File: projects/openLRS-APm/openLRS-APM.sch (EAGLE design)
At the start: 23 parts, among them IC2 RFM23BPSMD, J1 AVR_SPI_PRG_6PTH, U1 ATMEGA328P, Y1 16MHz

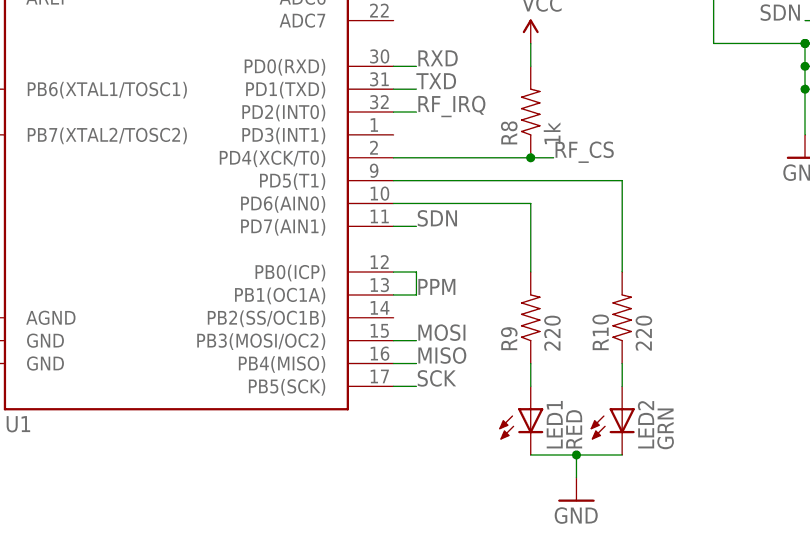
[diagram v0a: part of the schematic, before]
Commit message: Revert 0493923..5027763
This rolls back to commit 049392304cea7ab2cd1e886349edb191a1876f4a.
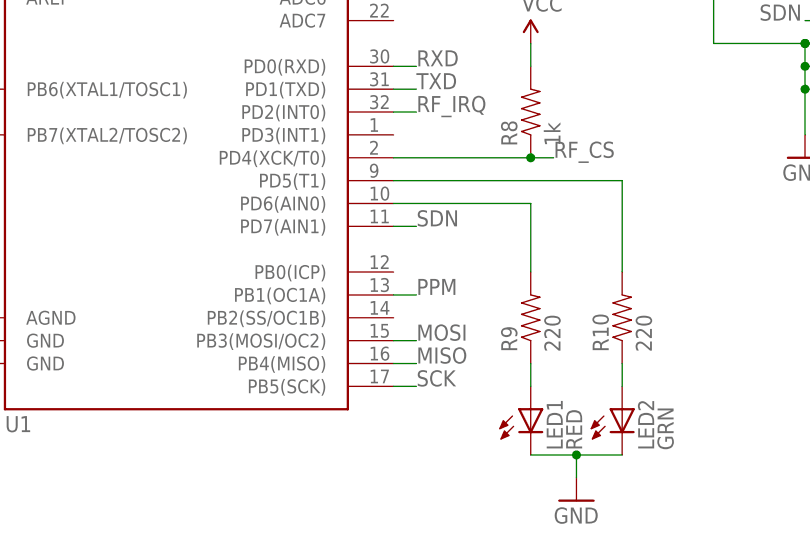
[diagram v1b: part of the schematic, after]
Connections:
- net PPM: no longer U1.PB0(ICP)
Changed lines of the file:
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@@
 <wire x1="91.44" y1="43.18" x2="93.98" y2="43.18" width="0.1524" layer="91"/>
 <label x="93.98" y="43.18" size="1.778" layer="95"/>
-<pinref part="U1" gate="G$1" pin="PB0(ICP)"/>
-<wire x1="93.98" y1="43.18" x2="93.98" y2="45.72" width="0.1524" layer="91"/>
-<wire x1="93.98" y1="45.72" x2="91.44" y2="45.72" width="0.1524" layer="91"/>
 </segment>
 </net>
